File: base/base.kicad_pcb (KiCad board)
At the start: 2 copper layers, 222.6 x 76 mm, 6 parts

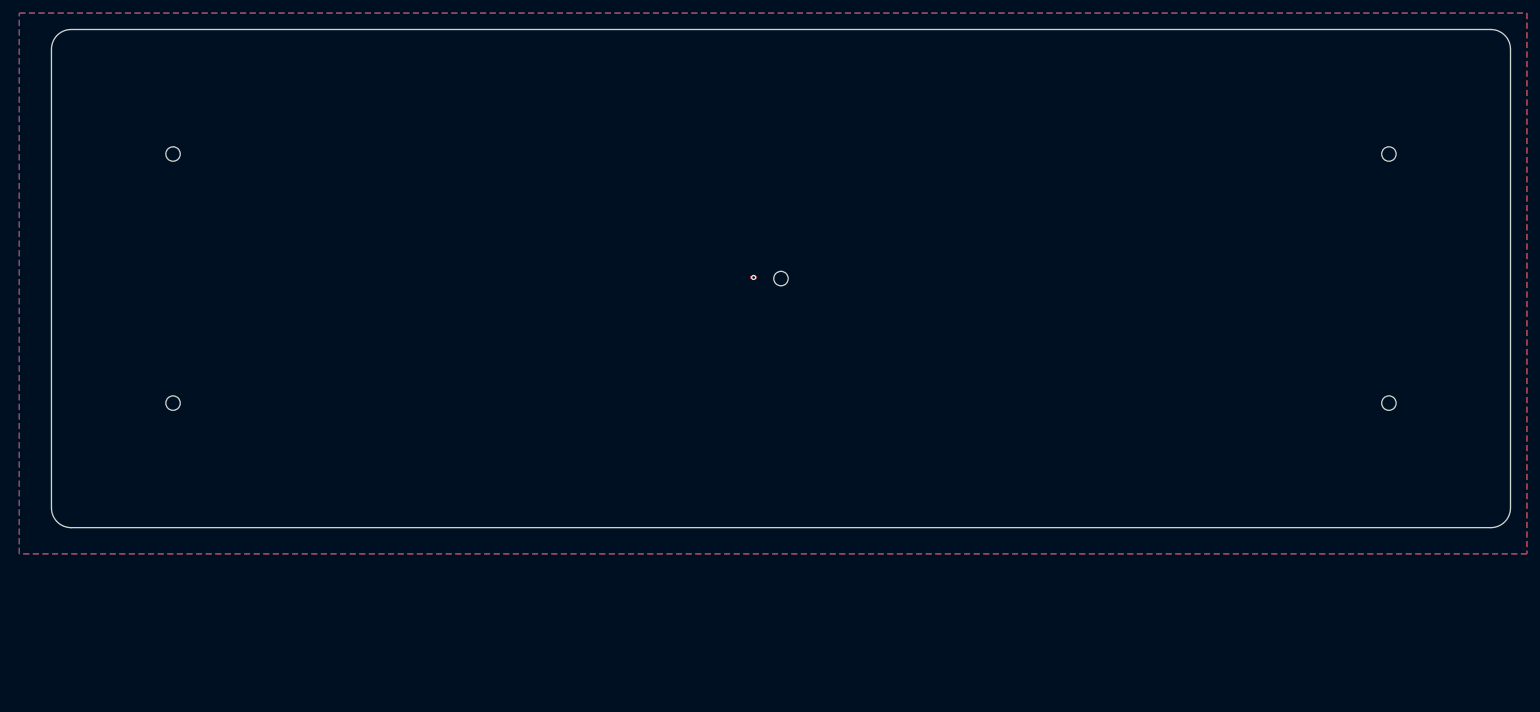
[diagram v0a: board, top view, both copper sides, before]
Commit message: adding base and plate
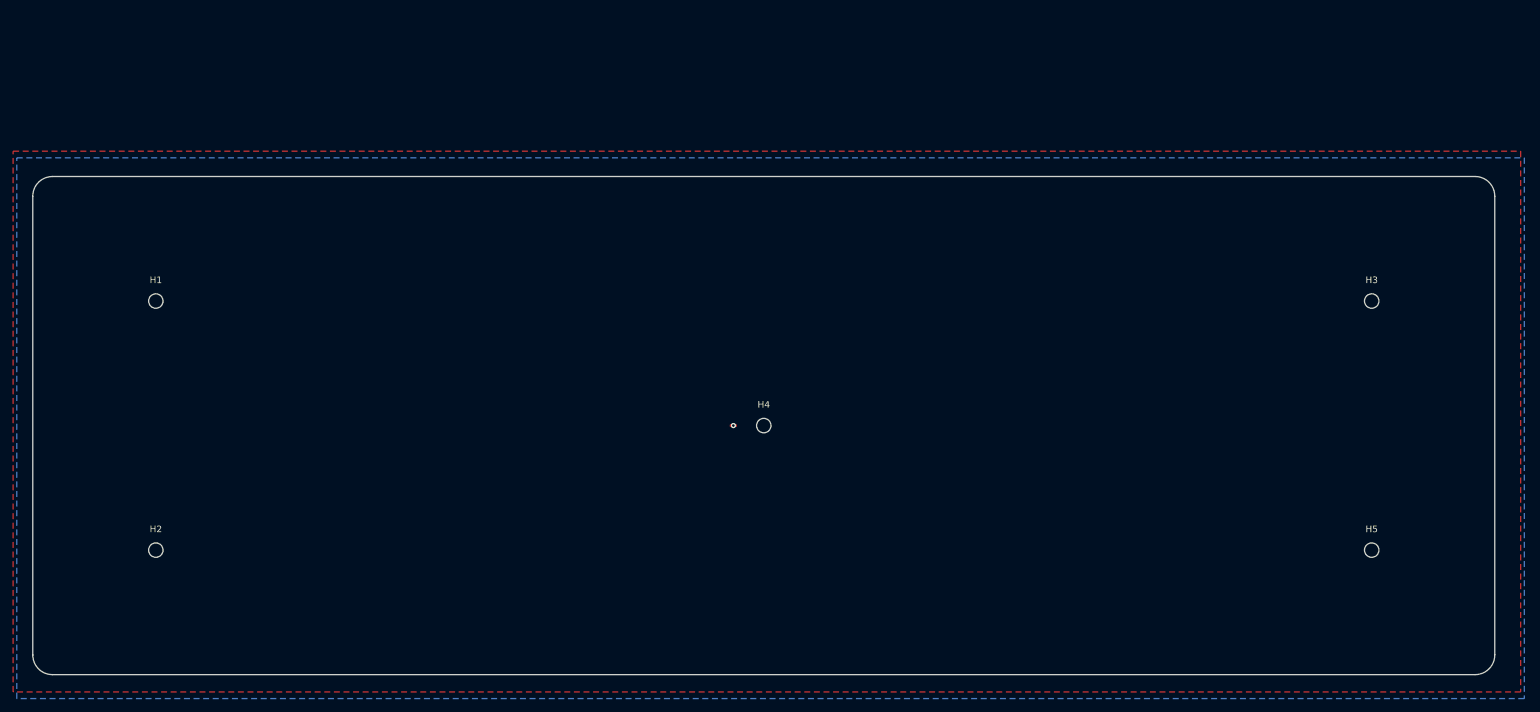
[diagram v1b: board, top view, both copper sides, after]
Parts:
- removed the   at (68.0, 44.0)
- removed the   at (68.0, 82.0)
- removed the   at (253.5, 44.0)
- removed the   at (160.7, 63.0)
- removed the   at (253.5, 82.0)
- added H1: MountingHole, MountingHole:MountingHole_2.2mm_M2, F.Cu at (65.3, 66.4)
- added H2: MountingHole, MountingHole:MountingHole_2.2mm_M2, F.Cu at (65.3, 104.4)
- added H3: MountingHole, MountingHole:MountingHole_2.2mm_M2, F.Cu at (250.8, 66.4)
- added H4: MountingHole, MountingHole:MountingHole_2.2mm_M2, F.Cu at (158.1, 85.4)
- added H5: MountingHole, MountingHole:MountingHole_2.2mm_M2, F.Cu at (250.8, 104.4)
- moved   22.8 mm to (153.5, 85.4)
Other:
- board size 222.6 x 76 mm -> 223 x 76 mm
